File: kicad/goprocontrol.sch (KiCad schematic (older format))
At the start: 37 parts, among them P1 CONN_01X06, Q1 MMBT3904, Q2 MMBT3904, Q3 MMBT3906, Q4 MMBT3906, Q5 IRLML6344, SW1 Reset, SW2 Prog, U1 NE555, U2 ESP-01v090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

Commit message: Design new v2.0 board
Still ESP8266 based
Add delaytimer v1.1 circuit for power control
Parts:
- removed CONN1: FTDI, synfinatic:FTDIHeader, symbol FTDI
- removed D1: B5817WS, Diodes_SMD:SOD-323_HandSoldering, symbol D_Schottky
- removed JP1: Jumper_NC_Dual, Connectors_JST:JST_EH_B03B-EH-A_03x2.50mm_Straight, symbol Jumper_NC_Dual
- removed R4: 10k, Resistors_SMD:R_0805_HandSoldering, symbol R
- removed R5: 22k, Resistors_SMD:R_0805_HandSoldering, symbol R
- added FTDIProg1: FTDI, synfinatic:FTDIHeader, symbol FTDI
- added P2: CONN_01X02, Pin_Headers:Pin_Header_Straight_1x02, symbol CONN_01X02
- SW1, SW2: footprint Buttons_Switches_SMD:SW_SPST_EVQPE1 -> synfinatic:SPST-SMD-6x3.5
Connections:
- net +12V: now also Q4.2 (E); no longer Q4.3 (C)
- net +3V3: now also P2.1 (P1)
- net GND: now also Q1.2 (E), FTDIProg1.6 (GND); no longer Q1.3 (C)
- net RXD: now also FTDIProg1.3 (TXD)
- net TXD: now also FTDIProg1.2 (RXI)
- net at C4.1, ROpt1.2, RV1.1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: now also Q1.3 (C); no longer Q1.2 (E)
- net at Q5.1 (G), R12.1: now also Q4.3 (C); no longer Q4.2 (E)
- new net: FTDIProg1.4 (VCC), P2.2 (P2)

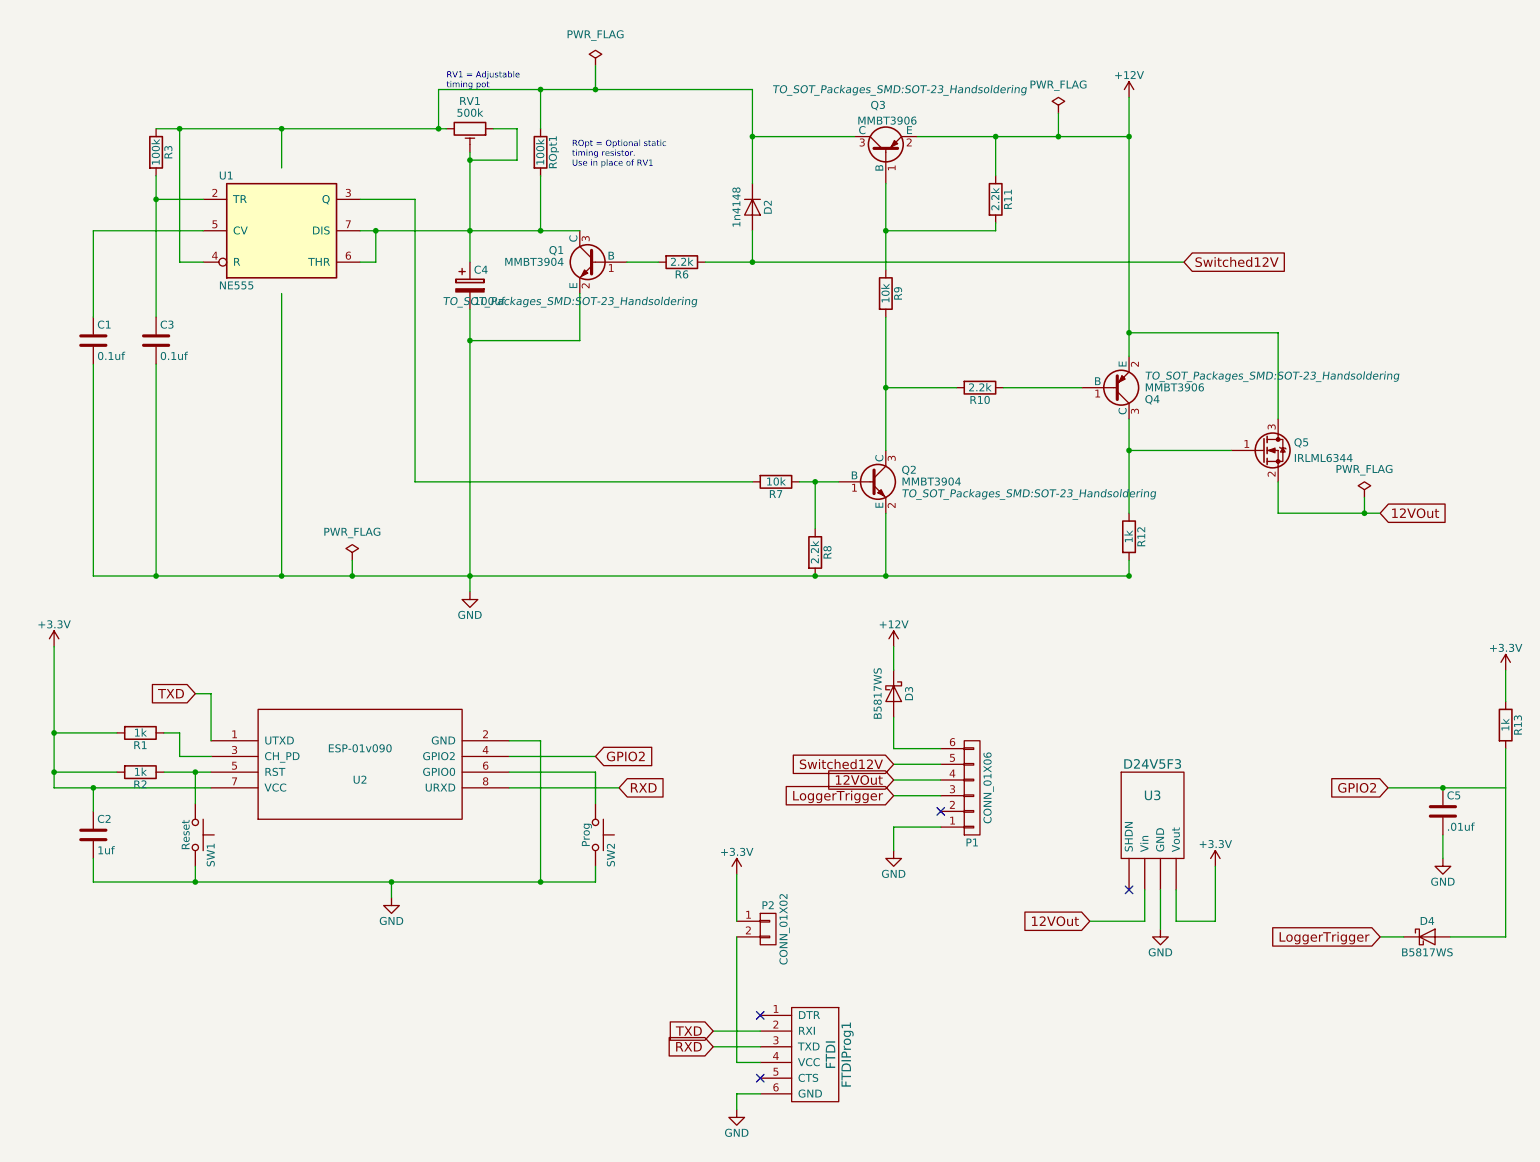
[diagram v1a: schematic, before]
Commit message: GoProControl v2.1 ordered
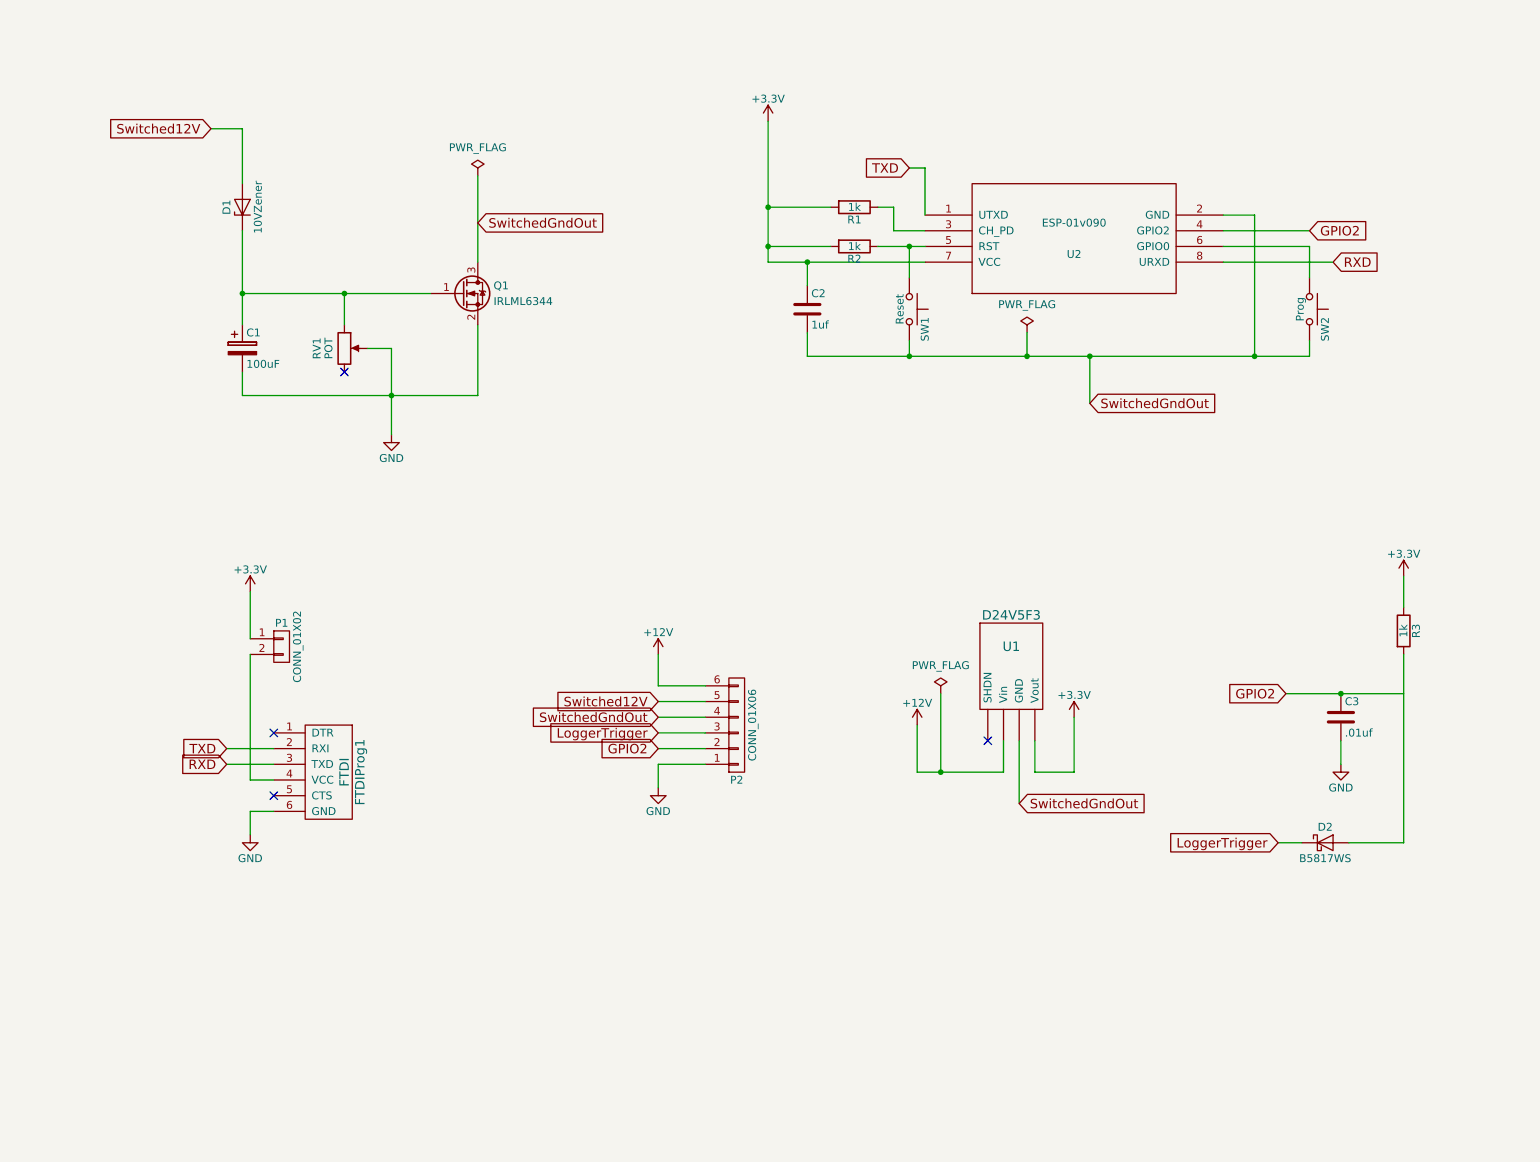
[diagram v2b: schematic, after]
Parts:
- removed C1, C3: 0.1uf, Capacitors_SMD:C_0805_HandSoldering, symbol C
- removed C4: 100uf, Capacitors_SMD:c_elec_6.3x7.7, symbol CP
- removed D2: 1n4148, Diodes_SMD:SOD-123, symbol D
- removed D3: B5817WS, Diodes_SMD:SOD-323_HandSoldering, symbol D_Schottky
- removed Q1, Q2: MMBT3904, TO_SOT_Packages_SMD:SOT-23_Handsoldering, symbol MMBT3904
- removed Q3, Q4: MMBT3906, TO_SOT_Packages_SMD:SOT-23_Handsoldering, symbol MMBT3906
- removed R10, R11, R6, R8: 2.2k, Resistors_SMD:R_0805_HandSoldering, symbol R
- removed R12: 1k, Resistors_SMD:R_0805_HandSoldering, symbol R
- removed R3, ROpt1: 100k, Resistors_SMD:R_0805_HandSoldering, symbol R
- removed R7, R9: 10k, Resistors_SMD:R_0805_HandSoldering, symbol R
- removed RV1: 500k, Potentiometers:Potentiometer_Bourns_3296W_3-8Zoll_Inline_ScrewUp, symbol POT_TRIM
- removed U1: NE555, Housings_SOIC:SOIC-8_3.9x4.9mm_Pitch1.27mm, symbol NE555
- added C1: 100uF, Capacitors_SMD:CP_Elec_6.3x7.7, symbol CP
- added D1: 10VZener, Diodes_SMD:D_SOD-123F, symbol D_Zener
- added RV1: POT, Potentiometers:Potentiometer_Bourns_3296W_3-8Zoll_Inline_ScrewUp, symbol POT
- P2: renamed from P1; footprint Connectors_Terminal_Blocks:TerminalBlock_Pheonix_PT-3.5mm_6pol -> Connectors_Phoenix:PhoenixContact_MC-G_06x5.08mm_Angled
- renumbered C5 to C3, D4 to D2, P2 to P1, Q5 to Q1, R13 to R3, U3 to U1
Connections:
- net +12V: now also P2.6 (P6), U1.2 (Vin); no longer Q1.3 (D)
- net GND: now also Q1.2 (S), C1.2, RV1.2; no longer C2.2, SW1.2, SW2.2, U1.3 (GND), U2.2 (GND)
- net GPIO2: now also P2.2 (P2)
- net Switched12V: now also D1.2 (A)
- net at Q1.1 (G): now also C1.1, D1.1 (K), RV1.1
- removed net 12VOut: P2.4 (P4), Q1.2 (S), U1.2 (Vin)
- new net SwitchedGndOut: C2.2, P2.4 (P4), Q1.3 (D), SW1.2, SW2.2, U1.3 (GND), U2.2 (GND)
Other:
- note removed: "ROpt = Optional static \ntiming resistor.\nUse in place of RV1"
- note removed: "RV1 = Adjustable\ntiming pot"
- moved on the sheet: C2, C3, D2, FTDIProg1, P1, P2, Q1, R1, R2, R3, SW1, SW2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

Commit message: Rev board to v2.2
- Switch to using ESP12E
- Switch to using OptoIsolator + ESP power off detection
- Using Pot to control power off delay
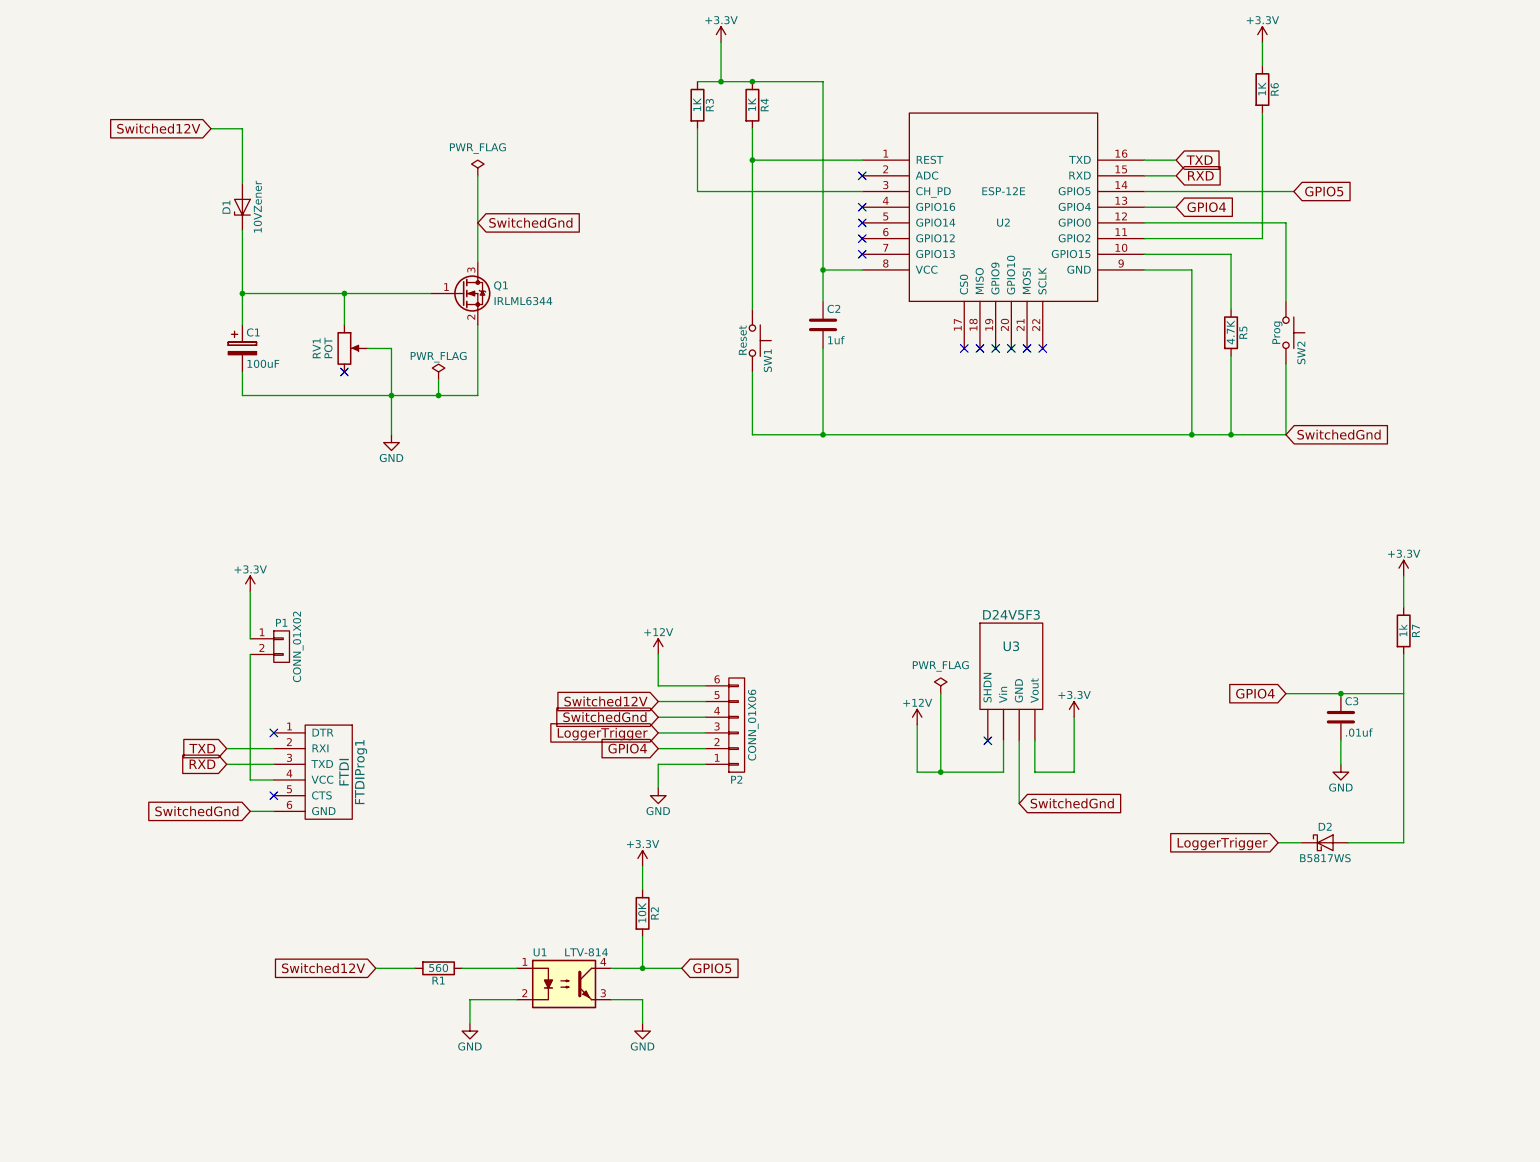
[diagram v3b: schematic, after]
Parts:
- removed U2: ESP-01v090, ESP8266:ESP-01, symbol ESP-01v090
- added R3, R4, R6: 1K, Resistors_SMD:R_0805_HandSoldering, symbol R
- added R5: 4.7K, Resistors_SMD:R_0805_HandSoldering, symbol R
- added U1: LTV-814, Opto-Devices:Optocoupler_SMD_LTV-817S, symbol LTV-814
- added U2: ESP-12E, synfinatic:ESP-12E-SMD, symbol ESP-12E
- R1: value 1k -> 560
- R2: value 1k -> 10K
- renumbered R3 to R7, U1 to U3
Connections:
- net +3V3: now also R2.1, R3.1, R4.1, R6.1, U2.8 (VCC); no longer R1.2, R2.2
- net GND: now also U1.2, U1.3; no longer FTDIProg1.6 (GND)
- net RXD: now also U2.15 (RXD)
- net Switched12V: now also R1.2
- net TXD: now also U2.16 (TXD)
- net at R1.1: now also U1.1
- net at SW1.1: now also R4.2, U2.1 (REST); no longer R2.1
- net at SW2.1: now also U2.12 (GPIO0)
- net GPIO2 renamed GPIO4
- net GPIO4: now also U2.13 (GPIO4)
- net SwitchedGndOut renamed SwitchedGnd
- net SwitchedGnd: now also FTDIProg1.6 (GND), R5.2, U2.9 (GND)
- new net: R5.1, U2.10 (GPIO15)
- new net: R6.2, U2.11 (GPIO2)
- new net: R3.2, U2.3 (CH_PD)
- new net GPIO5: R2.2, U1.4, U2.14 (GPIO5)
- no-connect marks 4 -> 15

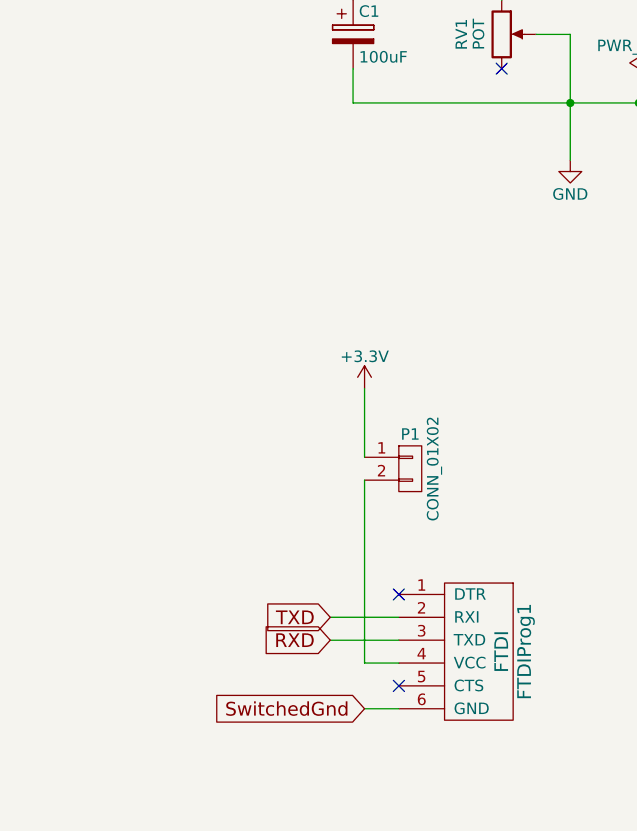
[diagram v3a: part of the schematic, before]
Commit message: v2.3 Board
- Larger holes for 1x6 connector
- Move 3.3V regulator out of the way
- clean up traces
- remove 3.3V FTDI selector
- Move Prog switch
- Better GND/SW-GND for MOSFET
- Add status LED
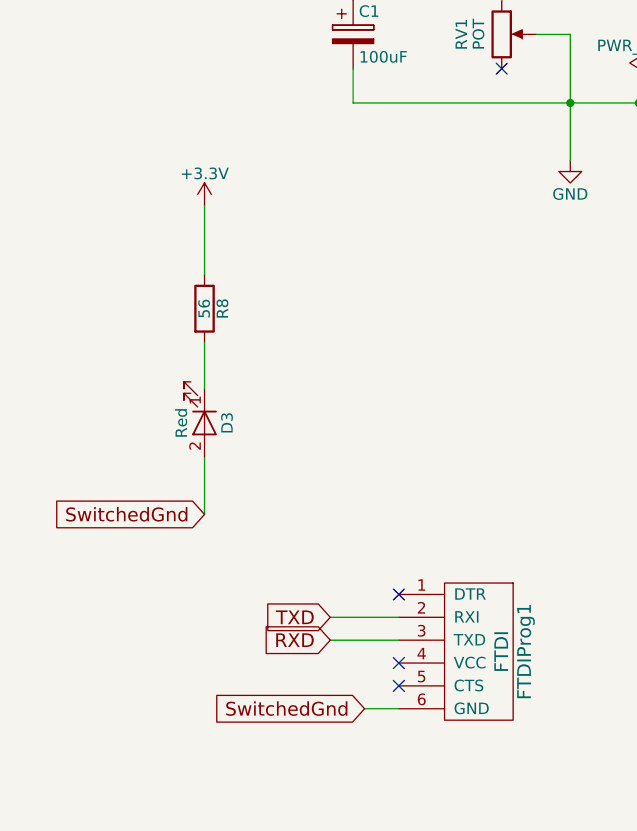
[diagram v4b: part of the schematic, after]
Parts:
- removed P1: CONN_01X02, Pin_Headers:Pin_Header_Straight_1x02, symbol CONN_01X02
- added D3: Red, LEDs:LED_0805_HandSoldering, symbol LED
- added R8: 56, Resistors_SMD:R_0805_HandSoldering, symbol R
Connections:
- net +3V3: now also R8.1
- net SwitchedGnd: now also D3.2 (A)
- new net: D3.1 (K), R8.2
- no-connect marks 15 -> 16
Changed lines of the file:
@@
 Sheet 1 1
 Title "GoProControl with Adjustable Delay Timer"
-Date "2018-02-17"
-Rev "v2.2"
+Date "2018-03-10"
+Rev "v2.3"
 Comp "Aaron Turner <synfinatic@gmail.com>"
 Comment1 "https://synfin.net/goprocontrol"
@@
 $EndComp
 $Comp
-L +3.3V #PWR06
-U 1 1 58B36D36
-P 2300 4300
-F 0 "#PWR06" H 2300 4150 50  0001 C CNN
-F 1 "+3.3V" H 2300 4440 50  0000 C CNN
-F 2 "" H 2300 4300 50  0000 C CNN
-F 3 "" H 2300 4300 50  0000 C CNN
-	1    2300 4300
-	1    0    0    -1
-$EndComp
-$Comp
-L CONN_01X02 P1
-U 1 1 58C4BF70
-P 2500 4650
-F 0 "P1" H 2500 4800 50  0000 C CNN
-F 1 "CONN_01X02" V 2600 4650 50  0000 C CNN
-F 2 "Pin_Headers:Pin_Header_Straight_1x02" H 2500 4650 50  0001 C CNN
-F 3 "" H 2500 4650 50  0000 C CNN
-	1    2500 4650
-	1    0    0    -1
-$EndComp
-$Comp
 L FTDI FTDIProg1
 U 1 1 58C4C044
@@
 $EndComp
 $Comp
-L GND #PWR07
+L GND #PWR06
 U 1 1 59D063DE
 P 3200 3300
-F 0 "#PWR07" H 3200 3050 50  0001 C CNN
+F 0 "#PWR06" H 3200 3050 50  0001 C CNN
 F 1 "GND" H 3200 3150 50  0000 C CNN
 F 2 "" H 3200 3300 50  0001 C CNN
@@
 Switched12V
 $Comp
-L GND #PWR08
+L GND #PWR07
 U 1 1 59D11961
 P 9250 5400
-F 0 "#PWR08" H 9250 5150 50  0001 C CNN
+F 0 "#PWR07" H 9250 5150 50  0001 C CNN
 F 1 "GND" H 9250 5250 50  0000 C CNN
 F 2 "" H 9250 5400 50  0001 C CNN
@@
 $EndComp
 $Comp
-L +12V #PWR09
+L +12V #PWR08
 U 1 1 59D11F12
 P 6550 5150
-F 0 "#PWR09" H 6550 5000 50  0001 C CNN
+F 0 "#PWR08" H 6550 5000 50  0001 C CNN
 F 1 "+12V" H 6550 5290 50  0000 C CNN
 F 2 "" H 6550 5150 50  0000 C CNN
@@
 	3750 3050 3750 2600
 Wire Wire Line
-	2300 5500 2450 5500
-Wire Wire Line
-	2300 4700 2300 5500
-Wire Wire Line
 	2450 5300 2150 5300
 Wire Wire Line
@@
 Wire Wire Line
 	2450 5400 2150 5400
-Wire Wire Line
-	2300 4300 2300 4600
 Wire Wire Line
 	2250 3050 3750 3050
@@
 NoConn ~ 2900 2900
 $Comp
-L PWR_FLAG #FLG010
+L PWR_FLAG #FLG09
 U 1 1 59D17FED
 P 6700 4950
-F 0 "#FLG010" H 6700 5045 50  0001 C CNN
+F 0 "#FLG09" H 6700 5045 50  0001 C CNN
 F 1 "PWR_FLAG" H 6700 5130 50  0000 C CNN
 F 2 "" H 6700 4950 50  0000 C CNN
@@
 	8300 2250 8000 2250
 $Comp
-L +3.3V #PWR011
+L +3.3V #PWR010
 U 1 1 5A88CFD8
 P 5300 800
-F 0 "#PWR011" H 5300 650 50  0001 C CNN
+F 0 "#PWR010" H 5300 650 50  0001 C CNN
 F 1 "+3.3V" H 5300 940 50  0000 C CNN
 F 2 "" H 5300 800 50  0001 C CNN
@@
 $EndComp
 $Comp
-L +3.3V #PWR012
+L +3.3V #PWR011
 U 1 1 5A88D00E
 P 8750 800
-F 0 "#PWR012" H 8750 650 50  0001 C CNN
+F 0 "#PWR011" H 8750 650 50  0001 C CNN
 F 1 "+3.3V" H 8750 940 50  0000 C CNN
 F 2 "" H 8750 800 50  0001 C CNN
@@
 	4800 6200 4800 6050
 $Comp
-L +3.3V #PWR013
+L +3.3V #PWR012
 U 1 1 5A88E492
 P 4800 6050
-F 0 "#PWR013" H 4800 5900 50  0001 C CNN
+F 0 "#PWR012" H 4800 5900 50  0001 C CNN
 F 1 "+3.3V" H 4800 6190 50  0000 C CNN
 F 2 "" H 4800 6050 50  0001 C CNN
@@
 $EndComp
 $Comp
-L GND #PWR014
+L GND #PWR013
 U 1 1 5A88E4DF
 P 4800 7050
-F 0 "#PWR014" H 4800 6800 50  0001 C CNN
+F 0 "#PWR013" H 4800 6800 50  0001 C CNN
 F 1 "GND" H 4800 6900 50  0000 C CNN
 F 2 "" H 4800 7050 50  0001 C CNN
@@
 GPIO5
 $Comp
-L GND #PWR015
+L GND #PWR014
 U 1 1 5A88E5E0
 P 3700 7050
-F 0 "#PWR015" H 3700 6800 50  0001 C CNN
+F 0 "#PWR014" H 3700 6800 50  0001 C CNN
 F 1 "GND" H 3700 6900 50  0000 C CNN
 F 2 "" H 3700 7050 50  0001 C CNN
@@
 	3700 6900 3700 7050
 $Comp
-L PWR_FLAG #FLG016
+L PWR_FLAG #FLG015
 U 1 1 5A88EF3E
 P 3500 2950
-F 0 "#FLG016" H 3500 3025 50  0001 C CNN
+F 0 "#FLG015" H 3500 3025 50  0001 C CNN
 F 1 "PWR_FLAG" H 3500 3100 50  0000 C CNN
 F 2 "" H 3500 2950 50  0001 C CNN
@@
 Text GLabel 2300 5700 0    60   Input ~ 0
 SwitchedGnd
+NoConn ~ 2450 5500
+$Comp
+L LED D3
+U 1 1 5AA4724E
+P 1600 4450
+F 0 "D3" H 1600 4550 50  0000 C CNN
+F 1 "Red" H 1600 4350 50  0000 C CNN
+F 2 "LEDs:LED_0805_HandSoldering" H 1600 4450 50  0001 C CNN
+F 3 "" H 1600 4450 50  0001 C CNN
+	1    1600 4450
+	0    1    1    0
+$EndComp
+$Comp
+L R R8
+U 1 1 5AA472B6
+P 1600 3950
+F 0 "R8" V 1680 3950 50  0000 C CNN
+F 1 "56" V 1600 3950 50  0000 C CNN
+F 2 "Resistors_SMD:R_0805_HandSoldering" V 1530 3950 50  0001 C CNN
+F 3 "" H 1600 3950 50  0001 C CNN
+	1    1600 3950
+	1    0    0    -1
+$EndComp
+$Comp
+L +3.3V #PWR016
+U 1 1 5AA4735E
+P 1600 3500
+F 0 "#PWR016" H 1600 3350 50  0001 C CNN
+F 1 "+3.3V" H 1600 3640 50  0000 C CNN
+F 2 "" H 1600 3500 50  0001 C CNN
+F 3 "" H 1600 3500 50  0001 C CNN
+	1    1600 3500
+	1    0    0    -1
+$EndComp
+Wire Wire Line
+	1600 3500 1600 3800
+Wire Wire Line
+	1600 4100 1600 4300
+Wire Wire Line
+	1600 4600 1600 4850
+Text GLabel 1600 4850 0    60   Input ~ 0
+SwitchedGnd
 $EndSCHEMATC
